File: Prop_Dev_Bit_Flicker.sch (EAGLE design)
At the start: 67 parts, among them J1 MF-CON-MICROUSB-RIGHT, J4 M20-7822046, J5 M20-7822046, U1 P8X32A-Q44, U2 FT230XQ-R, U3 TPS2113ADRBR, U4 CAT24C512WI-GT3, U5 MAX11613EUA+, U6 NCP1117LPST33T3G, U7 IRLML6401TRPBF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

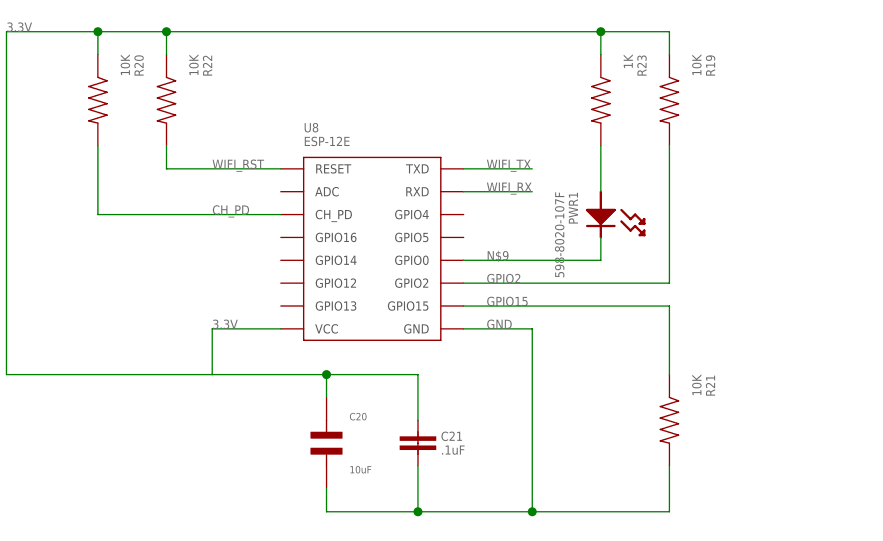
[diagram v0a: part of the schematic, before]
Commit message: top done. bottom next on silkscreen and trace clean u
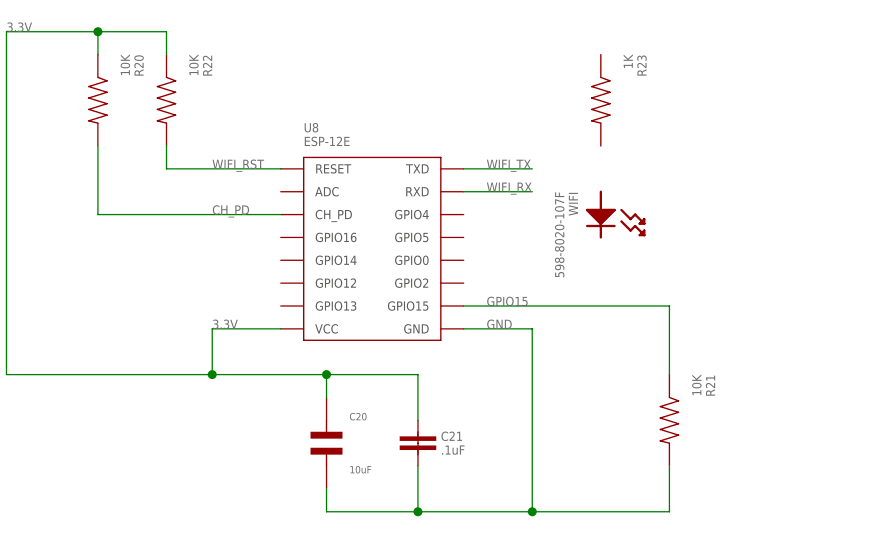
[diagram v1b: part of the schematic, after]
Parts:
- removed R19: 10K, PP_Passives:RESISTOR_0603
- renumbered PWR1 to WIFI
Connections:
- removed net GPIO2: R19.2, U8.GPIO2
- removed net N$4: R23.2, WIFI.ANODE
- removed net N$9: U8.GPIO0, WIFI.CATHODE
- net 3.3V: no longer R19.1, R23.1

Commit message: Finished REV 2. Added Fids.
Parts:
- removed R23: 1K, PP_Passives:RESISTOR_0603
- removed WIFI: 598-8020-107F, PP_LED:LED_SINGLE_0805
- added FID1, FID2, FID3, FID4: FIDUCIAL_0.5MM, MF_Aesthetics:FIDUCIAL_0.5MM
- U$1: REVNUM REV 1 -> REV 2
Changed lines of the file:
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@@
 <?xml version="1.0" encoding="utf-8"?>
 <!DOCTYPE eagle SYSTEM "eagle.dtd">
-<eagle version="7.5.0">
+<eagle version="7.4.0">
 <drawing>
 <settings>
@@
 <attribute name="DNAME" value="Parker Dillmann"/>
 <attribute name="PNAME" value="Propeller Development Bit Flicker"/>
-<attribute name="REVNUM" value="REV 1"/>
+<attribute name="REVNUM" value="REV 2"/>
 </part>
 <part name="U2" library="PP_DigitalIC" deviceset="FT230X" device="Q" value="FT230XQ-R"/>
@@
 <part name="R21" library="PP_Passives" deviceset="RESISTOR" device="_0603" value="10K"/>
 <part name="R22" library="PP_Passives" deviceset="RESISTOR" device="_0603" value="10K"/>
-<part name="WIFI" library="PP_LED" deviceset="LED_SINGLE" device="_0805" value="598-8020-107F "/>
-<part name="R23" library="PP_Passives" deviceset="RESISTOR" device="_0603" value="1K"/>
+<part name="FID1" library="MF_Aesthetics" deviceset="FIDUCIAL" device="_0.5MM"/>
+<part name="FID2" library="MF_Aesthetics" deviceset="FIDUCIAL" device="_0.5MM"/>
+<part name="FID3" library="MF_Aesthetics" deviceset="FIDUCIAL" device="_0.5MM"/>
+<part name="FID4" library="MF_Aesthetics" deviceset="FIDUCIAL" device="_0.5MM"/>
 </parts>
 <sheets>
@@
 <instance part="R21" gate="G$1" x="-58.42" y="307.34" rot="R270"/>
 <instance part="R22" gate="G$1" x="-114.3" y="342.9" rot="R270"/>
-<instance part="WIFI" gate="G$1" x="-66.04" y="330.2" rot="R270"/>
-<instance part="R23" gate="G$1" x="-66.04" y="342.9" rot="R270"/>
+<instance part="FID1" gate="G$1" x="-30.48" y="182.88"/>
+<instance part="FID2" gate="G$1" x="-30.48" y="187.96"/>
+<instance part="FID3" gate="G$1" x="-30.48" y="193.04"/>
+<instance part="FID4" gate="G$1" x="-30.48" y="198.12"/>
 </instances>
 <busses>

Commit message: Added DB
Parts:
- added U$3: DB_LOGO_SILK_SMALL, PP_Aesthetics:DB_LOGO_SILK_SMALL
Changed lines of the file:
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@@
 <part name="FID3" library="MF_Aesthetics" deviceset="FIDUCIAL" device="_0.5MM"/>
 <part name="FID4" library="MF_Aesthetics" deviceset="FIDUCIAL" device="_0.5MM"/>
+<part name="U$3" library="PP_Aesthetics" deviceset="DB_LOGO" device="_SILK_SMALL"/>
 </parts>
 <sheets>
@@
 <instance part="FID3" gate="G$1" x="-30.48" y="193.04"/>
 <instance part="FID4" gate="G$1" x="-30.48" y="198.12"/>
+<instance part="U$3" gate="G$1" x="-30.48" y="200.66" rot="MR180"/>
 </instances>
 <busses>

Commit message: Switch added to GPIO0 for the ESP-12E for flashing.
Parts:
- added PROG: EVP-BB2A1B000, PP_Electromechanical:SPST_EVPBB
- added R19: 10K, PP_Passives:RESISTOR_0603
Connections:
- removed net P26: J5.10, U1.P26
- removed net P27: J5.9, U1.P27
- new net GPIO0: PROG.A, R19.2, U8.GPIO0
- net 3.3V: now also R19.1
- net GND: now also PROG.B
- net WIFI_RX: now also J5.10, U1.P26
- net WIFI_TX: now also J5.9, U1.P27
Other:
- moved on the sheet: R21
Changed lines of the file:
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@@
 <part name="FID4" library="MF_Aesthetics" deviceset="FIDUCIAL" device="_0.5MM"/>
 <part name="U$3" library="PP_Aesthetics" deviceset="DB_LOGO" device="_SILK_SMALL"/>
+<part name="R19" library="PP_Passives" deviceset="RESISTOR" device="_0603" value="10K"/>
+<part name="PROG" library="PP_Electromechanical" deviceset="SPST" device="_EVPBB" value="EVP-BB2A1B000"/>
 </parts>
 <sheets>
@@
 <instance part="C21" gate="G$1" x="-86.36" y="304.8"/>
 <instance part="R20" gate="G$1" x="-121.92" y="342.9" rot="R270"/>
-<instance part="R21" gate="G$1" x="-58.42" y="307.34" rot="R270"/>
+<instance part="R21" gate="G$1" x="-68.58" y="307.34" rot="R270"/>
 <instance part="R22" gate="G$1" x="-114.3" y="342.9" rot="R270"/>
 <instance part="FID1" gate="G$1" x="-30.48" y="182.88"/>
@@
 <instance part="FID4" gate="G$1" x="-30.48" y="198.12"/>
 <instance part="U$3" gate="G$1" x="-30.48" y="200.66" rot="MR180"/>
+<instance part="R19" gate="G$1" x="-60.96" y="337.82" rot="R270"/>
+<instance part="PROG" gate="G$1" x="-60.96" y="307.34" rot="R270"/>
 </instances>
 <busses>
@@
 <junction x="-86.36" y="297.18"/>
 <pinref part="R21" gate="G$1" pin="2"/>
-<wire x1="-73.66" y1="297.18" x2="-58.42" y2="297.18" width="0.1524" layer="91"/>
-<wire x1="-58.42" y1="297.18" x2="-58.42" y2="302.26" width="0.1524" layer="91"/>
+<wire x1="-73.66" y1="297.18" x2="-68.58" y2="297.18" width="0.1524" layer="91"/>
+<wire x1="-68.58" y1="297.18" x2="-68.58" y2="302.26" width="0.1524" layer="91"/>
 <junction x="-73.66" y="297.18"/>
+<wire x1="-68.58" y1="297.18" x2="-60.96" y2="297.18" width="0.1524" layer="91"/>
+<pinref part="PROG" gate="G$1" pin="B"/>
+<wire x1="-60.96" y1="297.18" x2="-60.96" y2="302.26" width="0.1524" layer="91"/>
+<junction x="-68.58" y="297.18"/>
 </segment>
 </net>
@@
 <label x="-109.22" y="236.22" size="1.016" layer="95" font="vector"/>
 <pinref part="J5" gate="G$1" pin="8"/>
-</segment>
-</net>
-<net name="P27" class="0">
-<segment>
-<wire x1="-157.48" y1="233.68" x2="-144.78" y2="233.68" width="0.1524" layer="91"/>
-<label x="-147.32" y="233.68" size="1.016" layer="95" font="vector"/>
-<pinref part="U1" gate="G$1" pin="P27"/>
-</segment>
-<segment>
-<wire x1="-104.14" y1="233.68" x2="-109.22" y2="233.68" width="0.1524" layer="91"/>
-<label x="-109.22" y="233.68" size="1.016" layer="95" font="vector"/>
-<pinref part="J5" gate="G$1" pin="9"/>
-</segment>
-</net>
-<net name="P26" class="0">
-<segment>
-<wire x1="-144.78" y1="231.14" x2="-157.48" y2="231.14" width="0.1524" layer="91"/>
-<label x="-147.32" y="231.14" size="1.016" layer="95" font="vector"/>
-<pinref part="U1" gate="G$1" pin="P26"/>
-</segment>
-<segment>
-<wire x1="-109.22" y1="231.14" x2="-104.14" y2="231.14" width="0.1524" layer="91"/>
-<label x="-109.22" y="231.14" size="1.016" layer="95" font="vector"/>
-<pinref part="J5" gate="G$1" pin="10"/>
 </segment>
 </net>
@@
 <junction x="-121.92" y="350.52"/>
 <junction x="-109.22" y="312.42"/>
+<pinref part="R19" gate="G$1" pin="1"/>
+<wire x1="-60.96" y1="342.9" x2="-60.96" y2="350.52" width="0.1524" layer="91"/>
+<wire x1="-60.96" y1="350.52" x2="-114.3" y2="350.52" width="0.1524" layer="91"/>
+<junction x="-114.3" y="350.52"/>
 </segment>
 </net>
@@
 <label x="-78.74" y="335.28" size="1.016" layer="95" font="vector"/>
 </segment>
+<segment>
+<wire x1="-157.48" y1="233.68" x2="-144.78" y2="233.68" width="0.1524" layer="91"/>
+<label x="-147.32" y="233.68" size="1.016" layer="95" font="vector"/>
+<pinref part="U1" gate="G$1" pin="P27"/>
+</segment>
+<segment>
+<wire x1="-104.14" y1="233.68" x2="-109.22" y2="233.68" width="0.1524" layer="91"/>
+<label x="-109.22" y="233.68" size="1.016" layer="95" font="vector"/>
+<pinref part="J5" gate="G$1" pin="9"/>
+</segment>
 </net>
 <net name="WIFI_RX" class="0">
@@
 <label x="-78.74" y="332.74" size="1.016" layer="95" font="vector"/>
 </segment>
+<segment>
+<wire x1="-144.78" y1="231.14" x2="-157.48" y2="231.14" width="0.1524" layer="91"/>
+<label x="-147.32" y="231.14" size="1.016" layer="95" font="vector"/>
+<pinref part="U1" gate="G$1" pin="P26"/>
+</segment>
+<segment>
+<wire x1="-109.22" y1="231.14" x2="-104.14" y2="231.14" width="0.1524" layer="91"/>
+<label x="-109.22" y="231.14" size="1.016" layer="95" font="vector"/>
+<pinref part="J5" gate="G$1" pin="10"/>
+</segment>
 </net>
 <net name="GPIO15" class="0">
@@
 <label x="-78.74" y="320.04" size="1.016" layer="95" font="vector"/>
 <pinref part="R21" gate="G$1" pin="1"/>
-<wire x1="-81.28" y1="320.04" x2="-58.42" y2="320.04" width="0.1524" layer="91"/>
-<wire x1="-58.42" y1="320.04" x2="-58.42" y2="312.42" width="0.1524" layer="91"/>
+<wire x1="-81.28" y1="320.04" x2="-68.58" y2="320.04" width="0.1524" layer="91"/>
+<wire x1="-68.58" y1="320.04" x2="-68.58" y2="312.42" width="0.1524" layer="91"/>
 </segment>
 </net>
@@
 </segment>
 </net>
+<net name="GPIO0" class="0">
+<segment>
+<pinref part="U8" gate="G$1" pin="GPIO0"/>
+<pinref part="R19" gate="G$1" pin="2"/>
+<wire x1="-81.28" y1="325.12" x2="-60.96" y2="325.12" width="0.1524" layer="91"/>
+<wire x1="-60.96" y1="325.12" x2="-60.96" y2="332.74" width="0.1524" layer="91"/>
+<label x="-78.74" y="325.12" size="1.016" layer="95" font="vector"/>
+<pinref part="PROG" gate="G$1" pin="A"/>
+<wire x1="-60.96" y1="312.42" x2="-60.96" y2="325.12" width="0.1524" layer="91"/>
+<junction x="-60.96" y="325.12"/>
+</segment>
+</net>

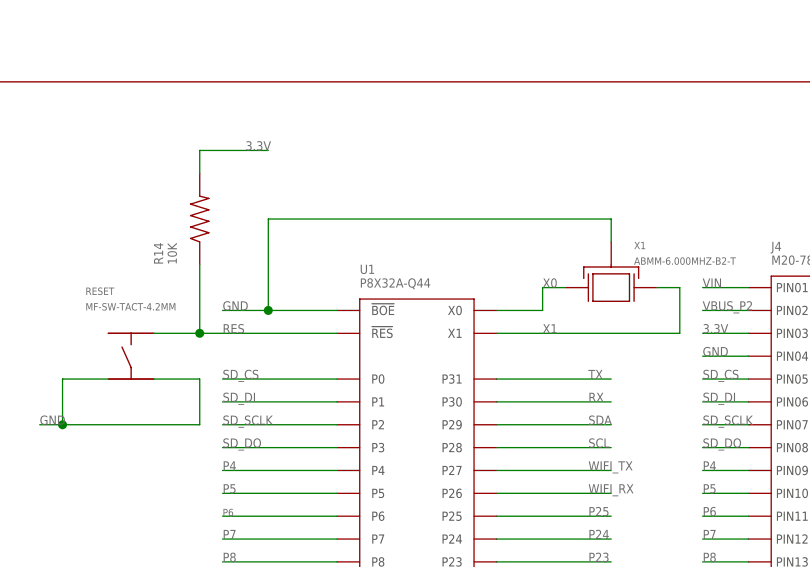
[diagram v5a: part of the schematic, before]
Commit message: Fixed part number for Prop to P8X32A-M44
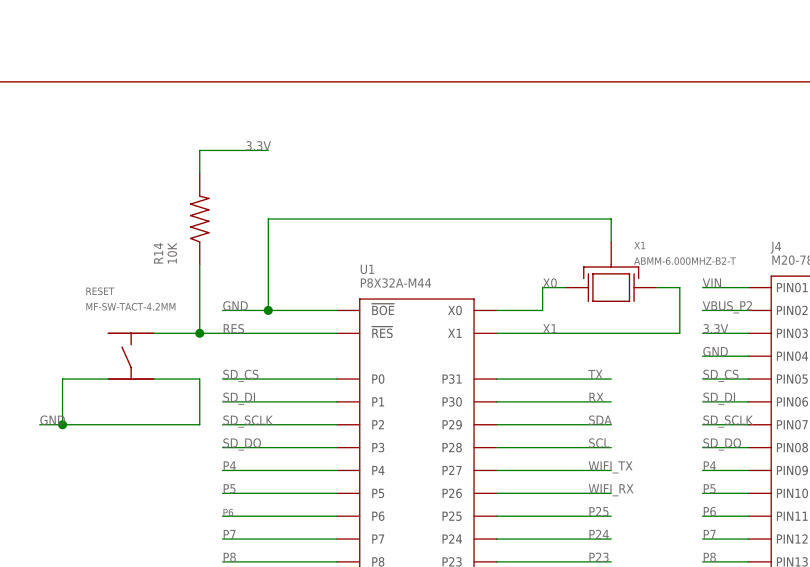
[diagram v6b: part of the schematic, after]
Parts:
- U1: value P8X32A-Q44 -> P8X32A-M44
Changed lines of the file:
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@@
 <part name="U5" library="PP_AnalogIC" deviceset="MAX11613" device="EUA+"/>
 <part name="U3" library="PP_PowerIC" deviceset="TPS211(2/3)" device="ADR" value="TPS2113ADRBR"/>
-<part name="U1" library="PP_DigitalIC" deviceset="P8X32A" device="-M44" value="P8X32A-Q44"/>
+<part name="U1" library="PP_DigitalIC" deviceset="P8X32A" device="-M44" value="P8X32A-M44"/>
 <part name="J2" library="PP_Connectors" deviceset="CON_01X04" device="_2.54MM_PIN_HEADER"/>
 <part name="J3" library="PP_Connectors" deviceset="CON_01X04" device="_2.54MM_PIN_HEADER"/>

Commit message: New Camfiles and added Tant Cap 100uF to 3.3V
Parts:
- added C22: F930J107MBA, PP_Passives:CAPACITOR_POLARIZED_CASE_B
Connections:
- net 3.3V: now also C22.POS
- net GND: now also C22.NEG
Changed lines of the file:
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@@
 <grid distance="0.1" unitdist="inch" unit="inch" style="lines" multiple="1" display="no" altdistance="0.01" altunitdist="inch" altunit="inch"/>
 <layers>
-<layer number="1" name="Top" color="4" fill="1" visible="no" active="no"/>
-<layer number="2" name="Route2" color="1" fill="3" visible="no" active="no"/>
-<layer number="3" name="Route3" color="4" fill="3" visible="no" active="no"/>
-<layer number="4" name="Route4" color="1" fill="4" visible="no" active="no"/>
-<layer number="5" name="Route5" color="4" fill="4" visible="no" active="no"/>
-<layer number="6" name="Route6" color="1" fill="8" visible="no" active="no"/>
-<layer number="7" name="Route7" color="4" fill="8" visible="no" active="no"/>
-<layer number="8" name="Route8" color="1" fill="2" visible="no" active="no"/>
-<layer number="9" name="Route9" color="4" fill="2" visible="no" active="no"/>
-<layer number="10" name="Route10" color="1" fill="7" visible="no" active="no"/>
-<layer number="11" name="Route11" color="4" fill="7" visible="no" active="no"/>
-<layer number="12" name="Route12" color="1" fill="5" visible="no" active="no"/>
-<layer number="13" name="Route13" color="4" fill="5" visible="no" active="no"/>
-<layer number="14" name="Route14" color="1" fill="6" visible="no" active="no"/>
-<layer number="15" name="Route15" color="4" fill="6" visible="no" active="no"/>
-<layer number="16" name="Bottom" color="1" fill="1" visible="no" active="no"/>
-<layer number="17" name="Pads" color="2" fill="1" visible="no" active="no"/>
-<layer number="18" name="Vias" color="2" fill="1" visible="no" active="no"/>
-<layer number="19" name="Unrouted" color="6" fill="1" visible="no" active="no"/>
-<layer number="20" name="Dimension" color="15" fill="1" visible="no" active="no"/>
-<layer number="21" name="tPlace" color="7" fill="1" visible="no" active="no"/>
-<layer number="22" name="bPlace" color="7" fill="1" visible="no" active="no"/>
-<layer number="23" name="tOrigins" color="15" fill="1" visible="no" active="no"/>
-<layer number="24" name="bOrigins" color="15" fill="1" visible="no" active="no"/>
-<layer number="25" name="tNames" color="7" fill="1" visible="no" active="no"/>
-<layer number="26" name="bNames" color="7" fill="1" visible="no" active="no"/>
-<layer number="27" name="tValues" color="7" fill="1" visible="no" active="no"/>
-<layer number="28" name="bValues" color="7" fill="1" visible="no" active="no"/>
+<layer number="1" name="Top" color="13" fill="1" visible="yes" active="no"/>
+<layer number="2" name="Route2" color="12" fill="0" visible="yes" active="no"/>
+<layer number="3" name="Route3" color="4" fill="3" visible="yes" active="no"/>
+<layer number="4" name="Route4" color="1" fill="4" visible="yes" active="no"/>
+<layer number="5" name="Route5" color="4" fill="4" visible="yes" active="no"/>
+<layer number="6" name="Route6" color="1" fill="8" visible="yes" active="no"/>
+<layer number="7" name="Route7" color="4" fill="8" visible="yes" active="no"/>
+<layer number="8" name="Route8" color="1" fill="2" visible="yes" active="no"/>
+<layer number="9" name="Route9" color="4" fill="2" visible="yes" active="no"/>
+<layer number="10" name="Route10" color="1" fill="7" visible="yes" active="no"/>
+<layer number="11" name="Route11" color="4" fill="7" visible="yes" active="no"/>
+<layer number="12" name="Route12" color="1" fill="5" visible="yes" active="no"/>
+<layer number="13" name="Route13" color="4" fill="5" visible="yes" active="no"/>
+<layer number="14" name="Route14" color="1" fill="6" visible="yes" active="no"/>
+<layer number="15" name="Route15" color="9" fill="0" visible="yes" active="no"/>
+<layer number="16" name="Bottom" color="14" fill="1" visible="yes" active="no"/>
+<layer number="17" name="Pads" color="2" fill="1" visible="yes" active="no"/>
+<layer number="18" name="Vias" color="2" fill="1" visible="yes" active="no"/>
+<layer number="19" name="Unrouted" color="6" fill="1" visible="yes" active="no"/>
+<layer number="20" name="Dimension" color="15" fill="1" visible="yes" active="no"/>
+<layer number="21" name="tPlace" color="7" fill="1" visible="yes" active="no"/>
+<layer number="22" name="bPlace" color="7" fill="1" visible="yes" active="no"/>
+<layer number="23" name="tOrigins" color="15" fill="1" visible="yes" active="no"/>
+<layer number="24" name="bOrigins" color="15" fill="1" visible="yes" active="no"/>
+<layer number="25" name="tNames" color="7" fill="1" visible="yes" active="no"/>
+<layer number="26" name="bNames" color="7" fill="1" visible="yes" active="no"/>
+<layer number="27" name="tValues" color="7" fill="1" visible="yes" active="no"/>
+<layer number="28" name="bValues" color="7" fill="1" visible="yes" active="no"/>
 <layer number="29" name="tStop" color="7" fill="3" visible="no" active="no"/>
 <layer number="30" name="bStop" color="7" fill="6" visible="no" active="no"/>
@@
 <layer number="35" name="tGlue" color="7" fill="4" visible="no" active="no"/>
 <layer number="36" name="bGlue" color="7" fill="5" visible="no" active="no"/>
-<layer number="37" name="tTest" color="7" fill="1" visible="no" active="no"/>
-<layer number="38" name="bTest" color="7" fill="1" visible="no" active="no"/>
+<layer number="37" name="tTest" color="7" fill="1" visible="yes" active="no"/>
+<layer number="38" name="bTest" color="7" fill="1" visible="yes" active="no"/>
 <layer number="39" name="tKeepout" color="4" fill="11" visible="no" active="no"/>
 <layer number="40" name="bKeepout" color="1" fill="11" visible="no" active="no"/>
@@
 <layer number="44" name="Drills" color="7" fill="1" visible="no" active="no"/>
 <layer number="45" name="Holes" color="7" fill="1" visible="no" active="no"/>
-<layer number="46" name="Milling" color="3" fill="1" visible="no" active="no"/>
-<layer number="47" name="Measures" color="7" fill="1" visible="no" active="no"/>
-<layer number="48" name="Document" color="7" fill="1" visible="no" active="no"/>
-<layer number="49" name="Reference" color="7" fill="1" visible="no" active="no"/>
-<layer number="50" name="dxf" color="7" fill="1" visible="no" active="no"/>
-<layer number="51" name="tDocu" color="7" fill="1" visible="no" active="no"/>
-<layer number="52" name="bDocu" color="7" fill="1" visible="no" active="no"/>
-<layer number="53" name="tGND_GNDA" color="7" fill="9" visible="no" active="no"/>
-<layer number="54" name="bGND_GNDA" color="1" fill="9" visible="no" active="no"/>
-<layer number="56" name="wert" color="7" fill="1" visible="no" active="no"/>
+<layer number="46" name="Milling" color="3" fill="1" visible="yes" active="no"/>
+<layer number="47" name="Measures" color="7" fill="1" visible="yes" active="no"/>
+<layer number="48" name="Document" color="7" fill="1" visible="yes" active="no"/>
+<layer number="49" name="Reference" color="7" fill="1" visible="yes" active="no"/>
+<layer number="50" name="dxf" color="7" fill="1" visible="yes" active="no"/>
+<layer number="51" name="tDocu" color="7" fill="1" visible="yes" active="no"/>
+<layer number="52" name="bDocu" color="7" fill="1" visible="yes" active="no"/>
+<layer number="53" name="tGND_GNDA" color="7" fill="9" visible="yes" active="no"/>
+<layer number="54" name="bGND_GNDA" color="1" fill="9" visible="yes" active="no"/>
+<layer number="56" name="wert" color="7" fill="1" visible="yes" active="no"/>
 <layer number="91" name="Nets" color="2" fill="1" visible="yes" active="yes"/>
 <layer number="92" name="Busses" color="1" fill="1" visible="yes" active="yes"/>
@@
 <part name="R19" library="PP_Passives" deviceset="RESISTOR" device="_0603" value="10K"/>
 <part name="PROG" library="PP_Electromechanical" deviceset="SPST" device="_EVPBB" value="EVP-BB2A1B000"/>
+<part name="C22" library="PP_Passives" deviceset="CAPACITOR_POLARIZED" device="_CASE_B" value="F930J107MBA"/>
 </parts>
 <sheets>
@@
 <instance part="R19" gate="G$1" x="-60.96" y="337.82" rot="R270"/>
 <instance part="PROG" gate="G$1" x="-60.96" y="307.34" rot="R270"/>
+<instance part="C22" gate="G$1" x="-101.6" y="304.8" rot="MR0"/>
 </instances>
 <busses>
@@
 <wire x1="-60.96" y1="297.18" x2="-60.96" y2="302.26" width="0.1524" layer="91"/>
 <junction x="-68.58" y="297.18"/>
+<pinref part="C22" gate="G$1" pin="NEG"/>
+<wire x1="-96.52" y1="297.18" x2="-101.6" y2="297.18" width="0.1524" layer="91"/>
+<wire x1="-101.6" y1="297.18" x2="-101.6" y2="302.26" width="0.1524" layer="91"/>
+<junction x="-96.52" y="297.18"/>
 </segment>
 </net>
@@
 <wire x1="-101.6" y1="317.5" x2="-109.22" y2="317.5" width="0.1524" layer="91"/>
 <wire x1="-109.22" y1="317.5" x2="-109.22" y2="312.42" width="0.1524" layer="91"/>
-<wire x1="-109.22" y1="312.42" x2="-96.52" y2="312.42" width="0.1524" layer="91"/>
+<wire x1="-109.22" y1="312.42" x2="-101.6" y2="312.42" width="0.1524" layer="91"/>
 <pinref part="C21" gate="G$1" pin="1"/>
+<wire x1="-101.6" y1="312.42" x2="-96.52" y2="312.42" width="0.1524" layer="91"/>
 <wire x1="-96.52" y1="312.42" x2="-86.36" y2="312.42" width="0.1524" layer="91"/>
 <wire x1="-86.36" y1="312.42" x2="-86.36" y2="307.34" width="0.1524" layer="91"/>
@@
 <wire x1="-60.96" y1="350.52" x2="-114.3" y2="350.52" width="0.1524" layer="91"/>
 <junction x="-114.3" y="350.52"/>
-</segment>
-</net>
+<pinref part="C22" gate="G$1" pin="POS"/>
+<wire x1="-101.6" y1="307.34" x2="-101.6" y2="312.42" width="0.1524" layer="91"/>
+<junction x="-101.6" y="312.42"/>
+</segment>
+</net>
